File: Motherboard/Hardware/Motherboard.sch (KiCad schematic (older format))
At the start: 0 parts

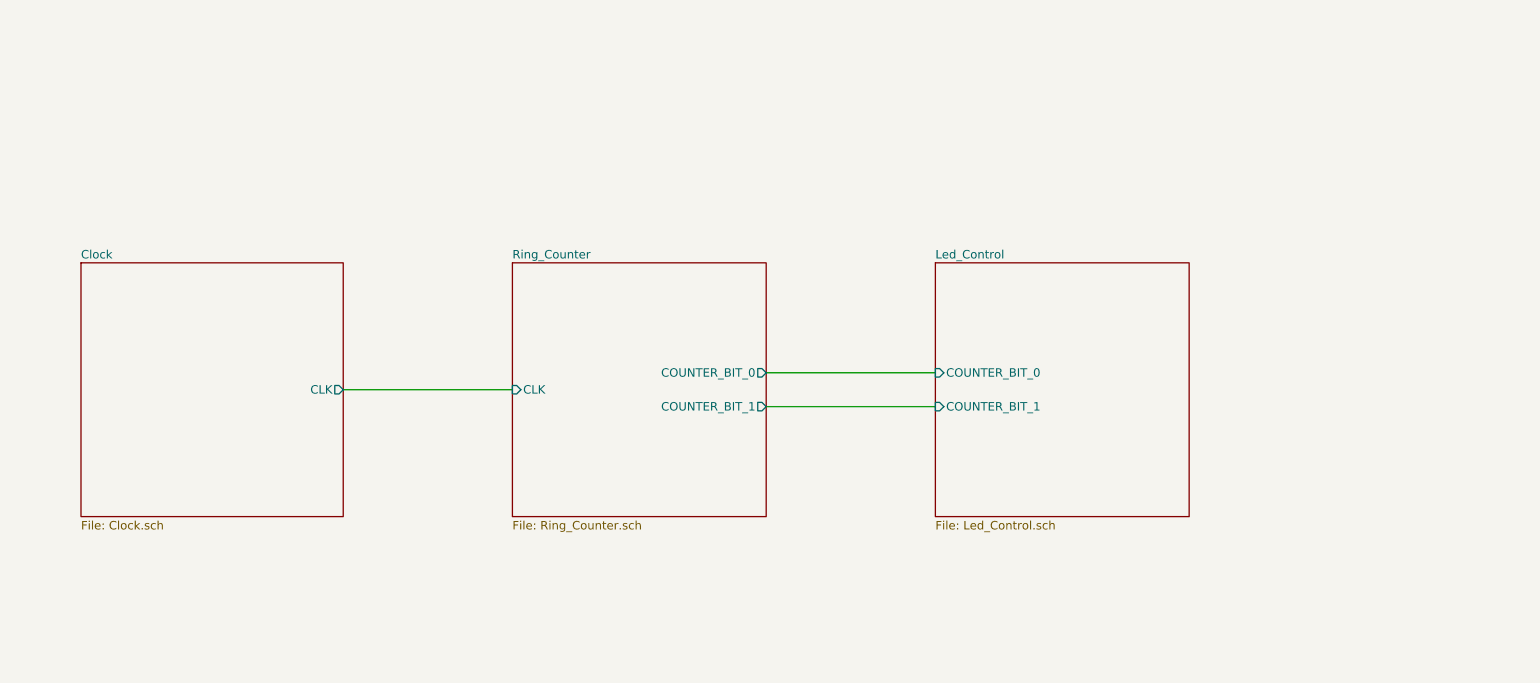
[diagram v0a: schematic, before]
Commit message: Added power supply and Christmas lights connectors to motherboard schematic.
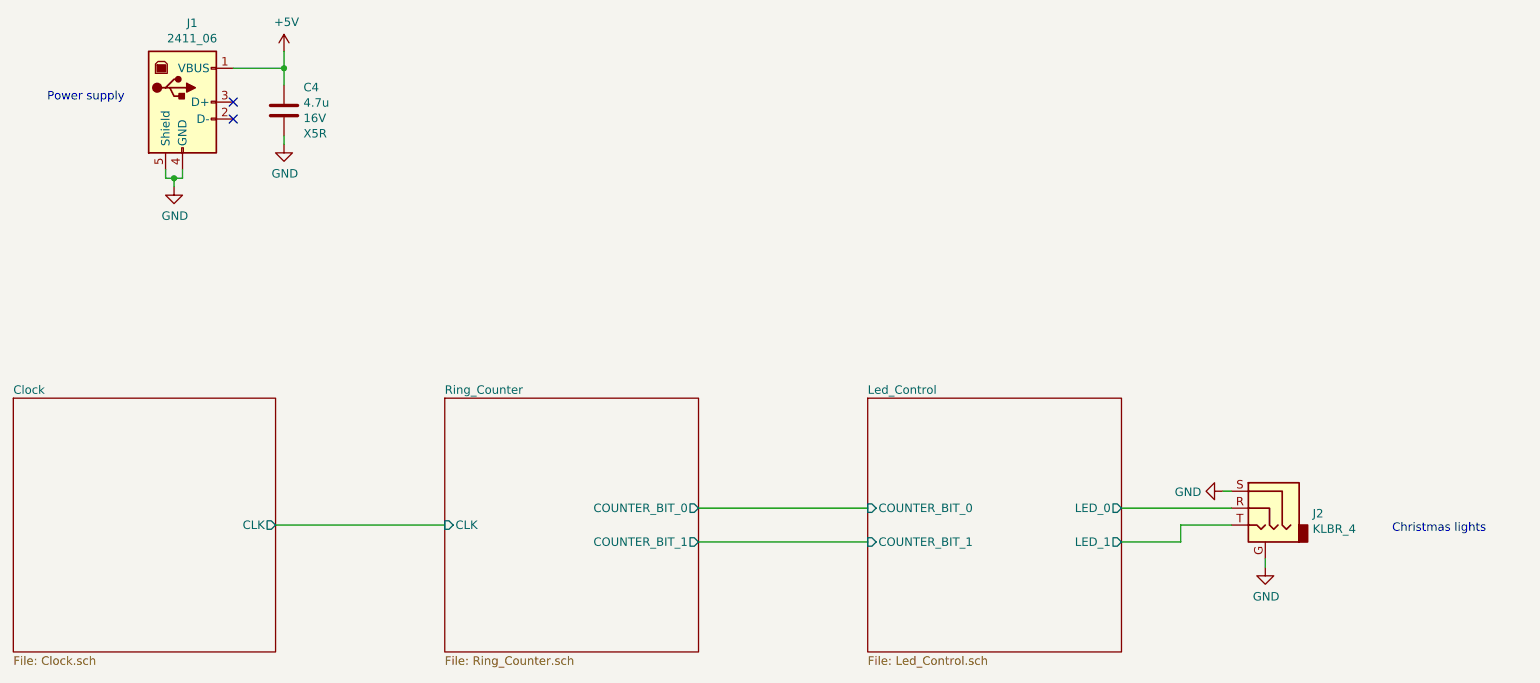
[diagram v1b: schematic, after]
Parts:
- added C4: 4.7u, Capacitor_SMD:C_0805_2012Metric_Pad1.18x1.45mm_HandSolder, symbol Device:C
- added J1: 2411_06, Connector_USB:USB_B_OST_USB-B1HSxx_Horizontal, symbol Connector:USB_B
- added J2: KLBR_4, KLBR_4:KLBR_4, symbol Connector:AudioJack3_Ground
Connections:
- new net +5V: C4.1, J1.1 (VBUS)
- new net GND: C4.2, J1.4 (GND), J1.5 (Shield), J2.G, J2.S
- new net Led_Control/LED_0: J2.R
- new net Led_Control/LED_1: J2.T
- no-connect marks 0 -> 2
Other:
- note added: "Christmas lights"
- note added: "Power supply"
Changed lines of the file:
@@
 $EndDescr
 $Sheet
-S 7050 3000 1500 1500
+S 6650 3800 1500 1500
 U 61CE6682
 F0 "Led_Control" 50
 F1 "Led_Control.sch" 50
-F2 "COUNTER_BIT_0" I L 7050 3650 50
-F3 "COUNTER_BIT_1" I L 7050 3850 50
+F2 "COUNTER_BIT_0" I L 6650 4450 50
+F3 "COUNTER_BIT_1" I L 6650 4650 50
+F4 "LED_0" O R 8150 4450 50
+F5 "LED_1" O R 8150 4650 50
 $EndSheet
 $Sheet
-S 4550 3000 1500 1500
+S 4150 3800 1500 1500
 U 61D90E9A
 F0 "Ring_Counter" 50
 F1 "Ring_Counter.sch" 50
-F2 "COUNTER_BIT_0" O R 6050 3650 50
-F3 "COUNTER_BIT_1" O R 6050 3850 50
-F4 "CLK" I L 4550 3750 50
+F2 "COUNTER_BIT_0" O R 5650 4450 50
+F3 "COUNTER_BIT_1" O R 5650 4650 50
+F4 "CLK" I L 4150 4550 50
 $EndSheet
 Wire Wire Line
-	6050 3650 7050 3650
+	5650 4450 6650 4450
 Wire Wire Line
-	7050 3850 6050 3850
+	6650 4650 5650 4650
 $Sheet
-S 2000 3000 1550 1500
+S 1600 3800 1550 1500
 U 622B55AD
 F0 "Clock" 50
 F1 "Clock.sch" 50
-F2 "CLK" O R 3550 3750 50
+F2 "CLK" O R 3150 4550 50
 $EndSheet
 Wire Wire Line
-	3550 3750 4550 3750
+	3150 4550 4150 4550
+$Comp
+L Connector:USB_B J1
+U 1 1 620ED163
+P 2600 2050
+F 0 "J1" H 2657 2517 50  0000 C CNN
+F 1 "2411_06" H 2657 2426 50  0000 C CNN
+F 2 "Connector_USB:USB_B_OST_USB-B1HSxx_Horizontal" H 2750 2000 50  0001 C CNN
+F 3 " ~" H 2750 2000 50  0001 C CNN
+F 4 "2411_06" H 2600 2050 50  0001 C CNN "PartNumber"
+F 5 "Lumberg" H 2600 2050 50  0001 C CNN "Manufacturer"
+	1    2600 2050
+	1    0    0    -1
+$EndComp
+NoConn ~ 2900 2050
+NoConn ~ 2900 2150
+$Comp
+L power:GND #PWR062
+U 1 1 620EEC8B
+P 2550 2550
+F 0 "#PWR062" H 2550 2300 50  0001 C CNN
+F 1 "GND" H 2555 2377 50  0000 C CNN
+F 2 "" H 2550 2550 50  0001 C CNN
+F 3 "" H 2550 2550 50  0001 C CNN
+	1    2550 2550
+	1    0    0    -1
+$EndComp
+Wire Wire Line
+	2500 2450 2500 2500
+Wire Wire Line
+	2500 2500 2550 2500
+Wire Wire Line
+	2550 2500 2550 2550
+Wire Wire Line
+	2550 2500 2600 2500
+Wire Wire Line
+	2600 2500 2600 2450
+Connection ~ 2550 2500
+$Comp
+L power:+5V #PWR05
+U 1 1 620F071B
+P 3200 1750
+F 0 "#PWR05" H 3200 1600 50  0001 C CNN
+F 1 "+5V" H 3215 1923 50  0000 C CNN
+F 2 "" H 3200 1750 50  0001 C CNN
+F 3 "" H 3200 1750 50  0001 C CNN
+	1    3200 1750
+	1    0    0    -1
+$EndComp
+Text Notes 1800 2050 0    50   ~ 0
+Power supply
+$Comp
+L Device:C C?
+U 1 1 620F4BED
+P 3200 2100
+AR Path="/61D90E9A/620F4BED" Ref="C?"  Part="1"
+AR Path="/622B55AD/620F4BED" Ref="C?"  Part="1"
+AR Path="/620F4BED" Ref="C4"  Part="1"
+F 0 "C4" H 3315 2237 50  0000 L CNN
+F 1 "4.7u" H 3315 2146 50  0000 L CNN
+F 2 "Capacitor_SMD:C_0805_2012Metric_Pad1.18x1.45mm_HandSolder" H 3238 1950 50  0001 C CNN
+F 3 "~" H 3200 2100 50  0001 C CNN
+F 4 "16V" H 3315 2055 50  0000 L CNN "Value2"
+F 5 "X5R" H 3315 1964 50  0000 L CNN "Value3"
+F 6 "CL21A475KOFNNNE" H 3200 2100 50  0001 C CNN "PartNumber"
+F 7 "Samsung" H 3200 2100 50  0001 C CNN "Manufacturer"
+	1    3200 2100
+	1    0    0    -1
+$EndComp
+$Comp
+L power:GND #PWR06
+U 1 1 620F5889
+P 3200 2300
+F 0 "#PWR06" H 3200 2050 50  0001 C CNN
+F 1 "GND" H 3205 2127 50  0000 C CNN
+F 2 "" H 3200 2300 50  0001 C CNN
+F 3 "" H 3200 2300 50  0001 C CNN
+	1    3200 2300
+	1    0    0    -1
+$EndComp
+Wire Wire Line
+	3200 2300 3200 2250
+Wire Wire Line
+	2900 1850 3200 1850
+Wire Wire Line
+	3200 1850 3200 1950
+Wire Wire Line
+	3200 1850 3200 1750
+Connection ~ 3200 1850
+$Comp
+L power:GND #PWR0101
+U 1 1 621289B2
+P 9000 4800
+F 0 "#PWR0101" H 9000 4550 50  0001 C CNN
+F 1 "GND" H 9005 4627 50  0000 C CNN
+F 2 "" H 9000 4800 50  0001 C CNN
+F 3 "" H 9000 4800 50  0001 C CNN
+	1    9000 4800
+	1    0    0    -1
+$EndComp
+$Comp
+L Connector:AudioJack3_Ground J2
+U 1 1 6212B914
+P 9000 4450
+F 0 "J2" H 8720 4418 50  0000 R CNN
+F 1 "KLBR_4" H 8720 4327 50  0000 R CNN
+F 2 "KLBR_4:KLBR_4" H 9000 4450 50  0001 C CNN
+F 3 "~" H 9000 4450 50  0001 C CNN
+F 4 "Lumberg" H 9000 4450 50  0001 C CNN "Manufacturer"
+F 5 "KLBR_4" H 9000 4450 50  0001 C CNN "PartNumber"
+	1    9000 4450
+	-1   0    0    -1
+$EndComp
+Wire Wire Line
+	9000 4800 9000 4750
+$Comp
+L power:GND #PWR0102
+U 1 1 6212F587
+P 8750 4350
+F 0 "#PWR0102" H 8750 4100 50  0001 C CNN
+F 1 "GND" V 8755 4222 50  0000 R CNN
+F 2 "" H 8750 4350 50  0001 C CNN
+F 3 "" H 8750 4350 50  0001 C CNN
+	1    8750 4350
+	0    1    1    0
+$EndComp
+Wire Wire Line
+	8750 4350 8800 4350
+Wire Wire Line
+	8150 4450 8800 4450
+Wire Wire Line
+	8500 4650 8500 4550
+Wire Wire Line
+	8500 4550 8800 4550
+Wire Wire Line
+	8150 4650 8500 4650
+Text Notes 9750 4600 0    50   ~ 0
+Christmas lights
 $EndSCHEMATC

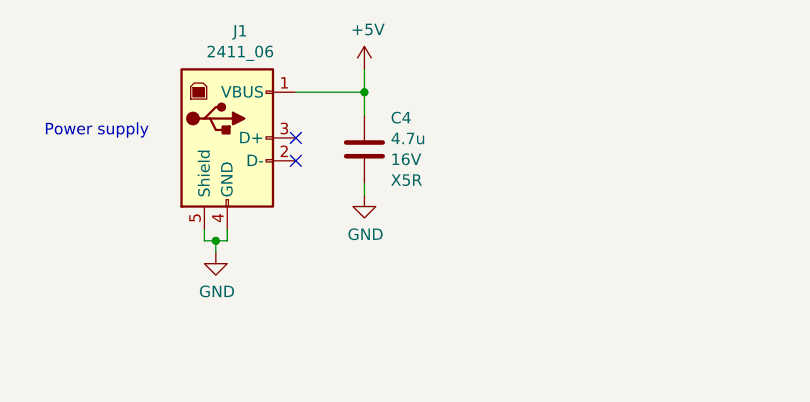
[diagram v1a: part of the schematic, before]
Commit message: Renamed all motherboard components so the name are ordered.
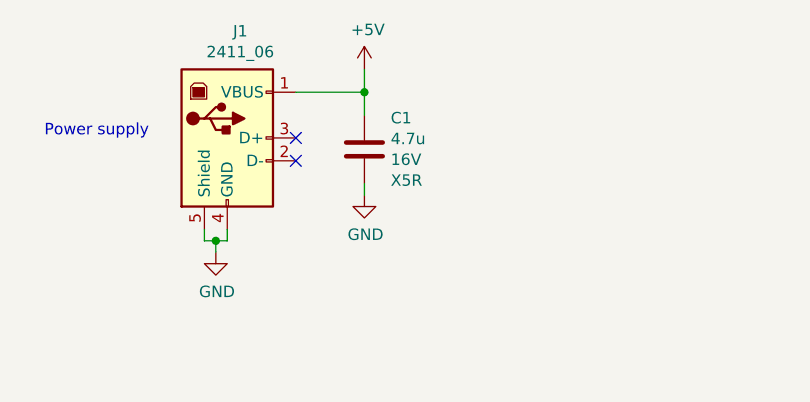
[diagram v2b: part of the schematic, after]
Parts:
- renumbered C4 to C1
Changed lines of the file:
@@
 NoConn ~ 2900 2150
 $Comp
-L power:GND #PWR062
+L power:GND #PWR03
 U 1 1 620EEC8B
 P 2550 2550
-F 0 "#PWR062" H 2550 2300 50  0001 C CNN
+F 0 "#PWR03" H 2550 2300 50  0001 C CNN
 F 1 "GND" H 2555 2377 50  0000 C CNN
 F 2 "" H 2550 2550 50  0001 C CNN
@@
 Connection ~ 2550 2500
 $Comp
-L power:+5V #PWR05
+L power:+5V #PWR01
 U 1 1 620F071B
 P 3200 1750
-F 0 "#PWR05" H 3200 1600 50  0001 C CNN
+F 0 "#PWR01" H 3200 1600 50  0001 C CNN
 F 1 "+5V" H 3215 1923 50  0000 C CNN
 F 2 "" H 3200 1750 50  0001 C CNN
@@
 AR Path="/61D90E9A/620F4BED" Ref="C?"  Part="1"
 AR Path="/622B55AD/620F4BED" Ref="C?"  Part="1"
-AR Path="/620F4BED" Ref="C4"  Part="1"
-F 0 "C4" H 3315 2237 50  0000 L CNN
+AR Path="/620F4BED" Ref="C1"  Part="1"
+F 0 "C1" H 3315 2237 50  0000 L CNN
 F 1 "4.7u" H 3315 2146 50  0000 L CNN
 F 2 "Capacitor_SMD:C_0805_2012Metric_Pad1.18x1.45mm_HandSolder" H 3238 1950 50  0001 C CNN
@@
 $EndComp
 $Comp
-L power:GND #PWR06
+L power:GND #PWR02
 U 1 1 620F5889
 P 3200 2300
-F 0 "#PWR06" H 3200 2050 50  0001 C CNN
+F 0 "#PWR02" H 3200 2050 50  0001 C CNN
 F 1 "GND" H 3205 2127 50  0000 C CNN
 F 2 "" H 3200 2300 50  0001 C CNN
@@
 Connection ~ 3200 1850
 $Comp
-L power:GND #PWR0101
+L power:GND #PWR05
 U 1 1 621289B2
 P 9000 4800
-F 0 "#PWR0101" H 9000 4550 50  0001 C CNN
+F 0 "#PWR05" H 9000 4550 50  0001 C CNN
 F 1 "GND" H 9005 4627 50  0000 C CNN
 F 2 "" H 9000 4800 50  0001 C CNN
@@
 	9000 4800 9000 4750
 $Comp
-L power:GND #PWR0102
+L power:GND #PWR04
 U 1 1 6212F587
 P 8750 4350
-F 0 "#PWR0102" H 8750 4100 50  0001 C CNN
+F 0 "#PWR04" H 8750 4100 50  0001 C CNN
 F 1 "GND" V 8755 4222 50  0000 R CNN
 F 2 "" H 8750 4350 50  0001 C CNN

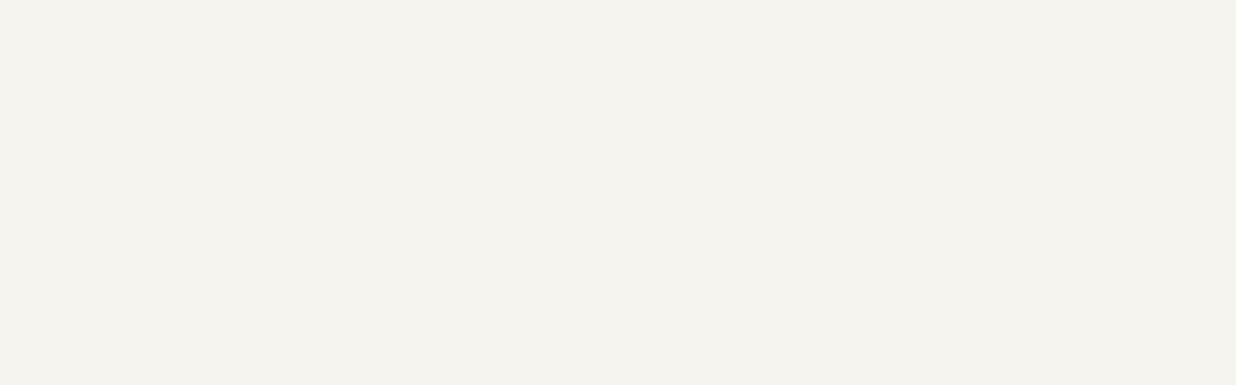
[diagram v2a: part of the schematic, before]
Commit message: Placed most of the components on the PCB.
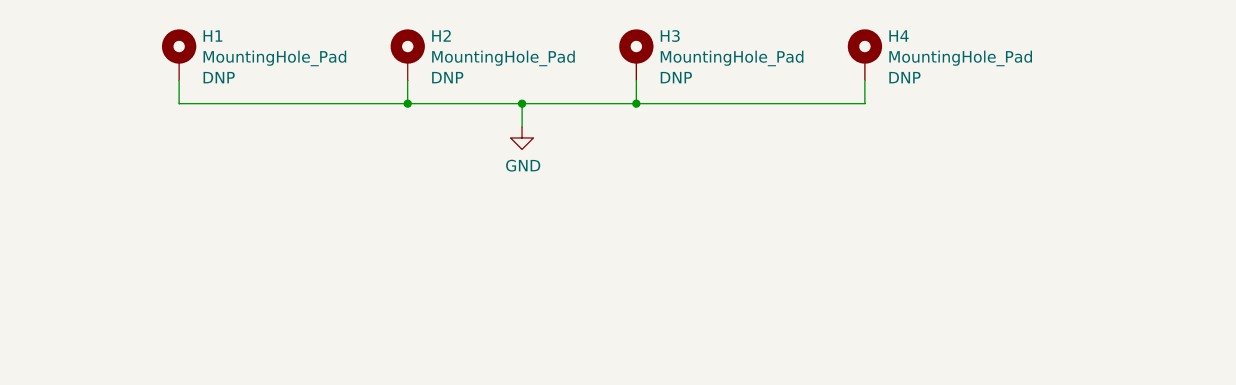
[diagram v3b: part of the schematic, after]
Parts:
- added H1, H2, H3, H4: MountingHole_Pad, MountingHole:MountingHole_4.5mm_Pad, symbol Mechanical:MountingHole_Pad
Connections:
- net GND: now also H1.1, H2.1, H3.1, H4.1
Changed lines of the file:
@@
 Text Notes 9750 4600 0    50   ~ 0
 Christmas lights
+$Comp
+L Mechanical:MountingHole_Pad H1
+U 1 1 6228BA0E
+P 5150 1700
+F 0 "H1" H 5250 1794 50  0000 L CNN
+F 1 "MountingHole_Pad" H 5250 1703 50  0000 L CNN
+F 2 "MountingHole:MountingHole_4.5mm_Pad" H 5150 1700 50  0001 C CNN
+F 3 "~" H 5150 1700 50  0001 C CNN
+F 4 "DNP" H 5250 1612 50  0000 L CNN "Populate"
+	1    5150 1700
+	1    0    0    -1
+$EndComp
+$Comp
+L Mechanical:MountingHole_Pad H2
+U 1 1 6228D4C8
+P 6150 1700
+F 0 "H2" H 6250 1794 50  0000 L CNN
+F 1 "MountingHole_Pad" H 6250 1703 50  0000 L CNN
+F 2 "MountingHole:MountingHole_4.5mm_Pad" H 6150 1700 50  0001 C CNN
+F 3 "~" H 6150 1700 50  0001 C CNN
+F 4 "DNP" H 6250 1612 50  0000 L CNN "Populate"
+	1    6150 1700
+	1    0    0    -1
+$EndComp
+$Comp
+L Mechanical:MountingHole_Pad H3
+U 1 1 6228D877
+P 7150 1700
+F 0 "H3" H 7250 1794 50  0000 L CNN
+F 1 "MountingHole_Pad" H 7250 1703 50  0000 L CNN
+F 2 "MountingHole:MountingHole_4.5mm_Pad" H 7150 1700 50  0001 C CNN
+F 3 "~" H 7150 1700 50  0001 C CNN
+F 4 "DNP" H 7250 1612 50  0000 L CNN "Populate"
+	1    7150 1700
+	1    0    0    -1
+$EndComp
+$Comp
+L Mechanical:MountingHole_Pad H4
+U 1 1 6228DDEA
+P 8150 1700
+F 0 "H4" H 8250 1794 50  0000 L CNN
+F 1 "MountingHole_Pad" H 8250 1703 50  0000 L CNN
+F 2 "MountingHole:MountingHole_4.5mm_Pad" H 8150 1700 50  0001 C CNN
+F 3 "~" H 8150 1700 50  0001 C CNN
+F 4 "DNP" H 8250 1612 50  0000 L CNN "Populate"
+	1    8150 1700
+	1    0    0    -1
+$EndComp
+$Comp
+L power:GND #PWR063
+U 1 1 62294043
+P 6650 2000
+F 0 "#PWR063" H 6650 1750 50  0001 C CNN
+F 1 "GND" H 6655 1827 50  0000 C CNN
+F 2 "" H 6650 2000 50  0001 C CNN
+F 3 "" H 6650 2000 50  0001 C CNN
+	1    6650 2000
+	1    0    0    -1
+$EndComp
+Wire Wire Line
+	5150 1800 5150 1900
+Wire Wire Line
+	5150 1900 6150 1900
+Wire Wire Line
+	6150 1900 6150 1800
+Connection ~ 6150 1900
+Wire Wire Line
+	6150 1900 6650 1900
+Wire Wire Line
+	7150 1900 7150 1800
+Wire Wire Line
+	7150 1900 8150 1900
+Wire Wire Line
+	8150 1900 8150 1800
+Connection ~ 7150 1900
+Wire Wire Line
+	6650 2000 6650 1900
+Connection ~ 6650 1900
+Wire Wire Line
+	6650 1900 7150 1900
 $EndSCHEMATC

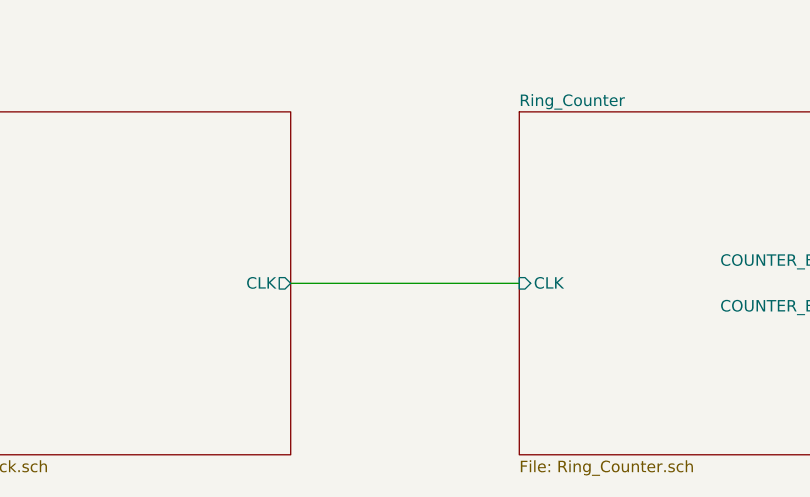
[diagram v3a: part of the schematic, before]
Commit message: Disabled the motherboard clock circuit power supply while power-on reset delay is running to avoid clocking the RS gates while they are being reset by the power-on reset.
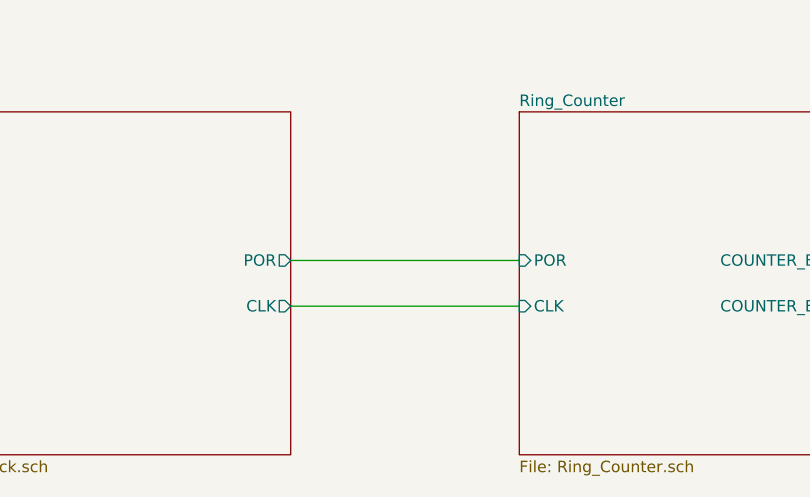
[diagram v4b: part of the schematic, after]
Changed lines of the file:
@@
 F2 "COUNTER_BIT_0" O R 5650 4450 50
 F3 "COUNTER_BIT_1" O R 5650 4650 50
-F4 "CLK" I L 4150 4550 50
+F4 "CLK" I L 4150 4650 50
+F5 "POR" I L 4150 4450 50
 $EndSheet
 Wire Wire Line
@@
 F0 "Clock" 50
 F1 "Clock.sch" 50
-F2 "CLK" O R 3150 4550 50
+F2 "CLK" O R 3150 4650 50
+F3 "POR" O R 3150 4450 50
 $EndSheet
 Wire Wire Line
-	3150 4550 4150 4550
+	3150 4650 4150 4650
 $Comp
 L Connector:USB_B J1
@@
 Wire Wire Line
 	6650 1900 7150 1900
+Wire Wire Line
+	3150 4450 4150 4450
 $EndSCHEMATC
